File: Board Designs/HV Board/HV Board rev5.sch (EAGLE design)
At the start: 95 parts, among them IC1 OKI-78SR, IC2 NE5532SOIC, IC3 NE5532SOIC

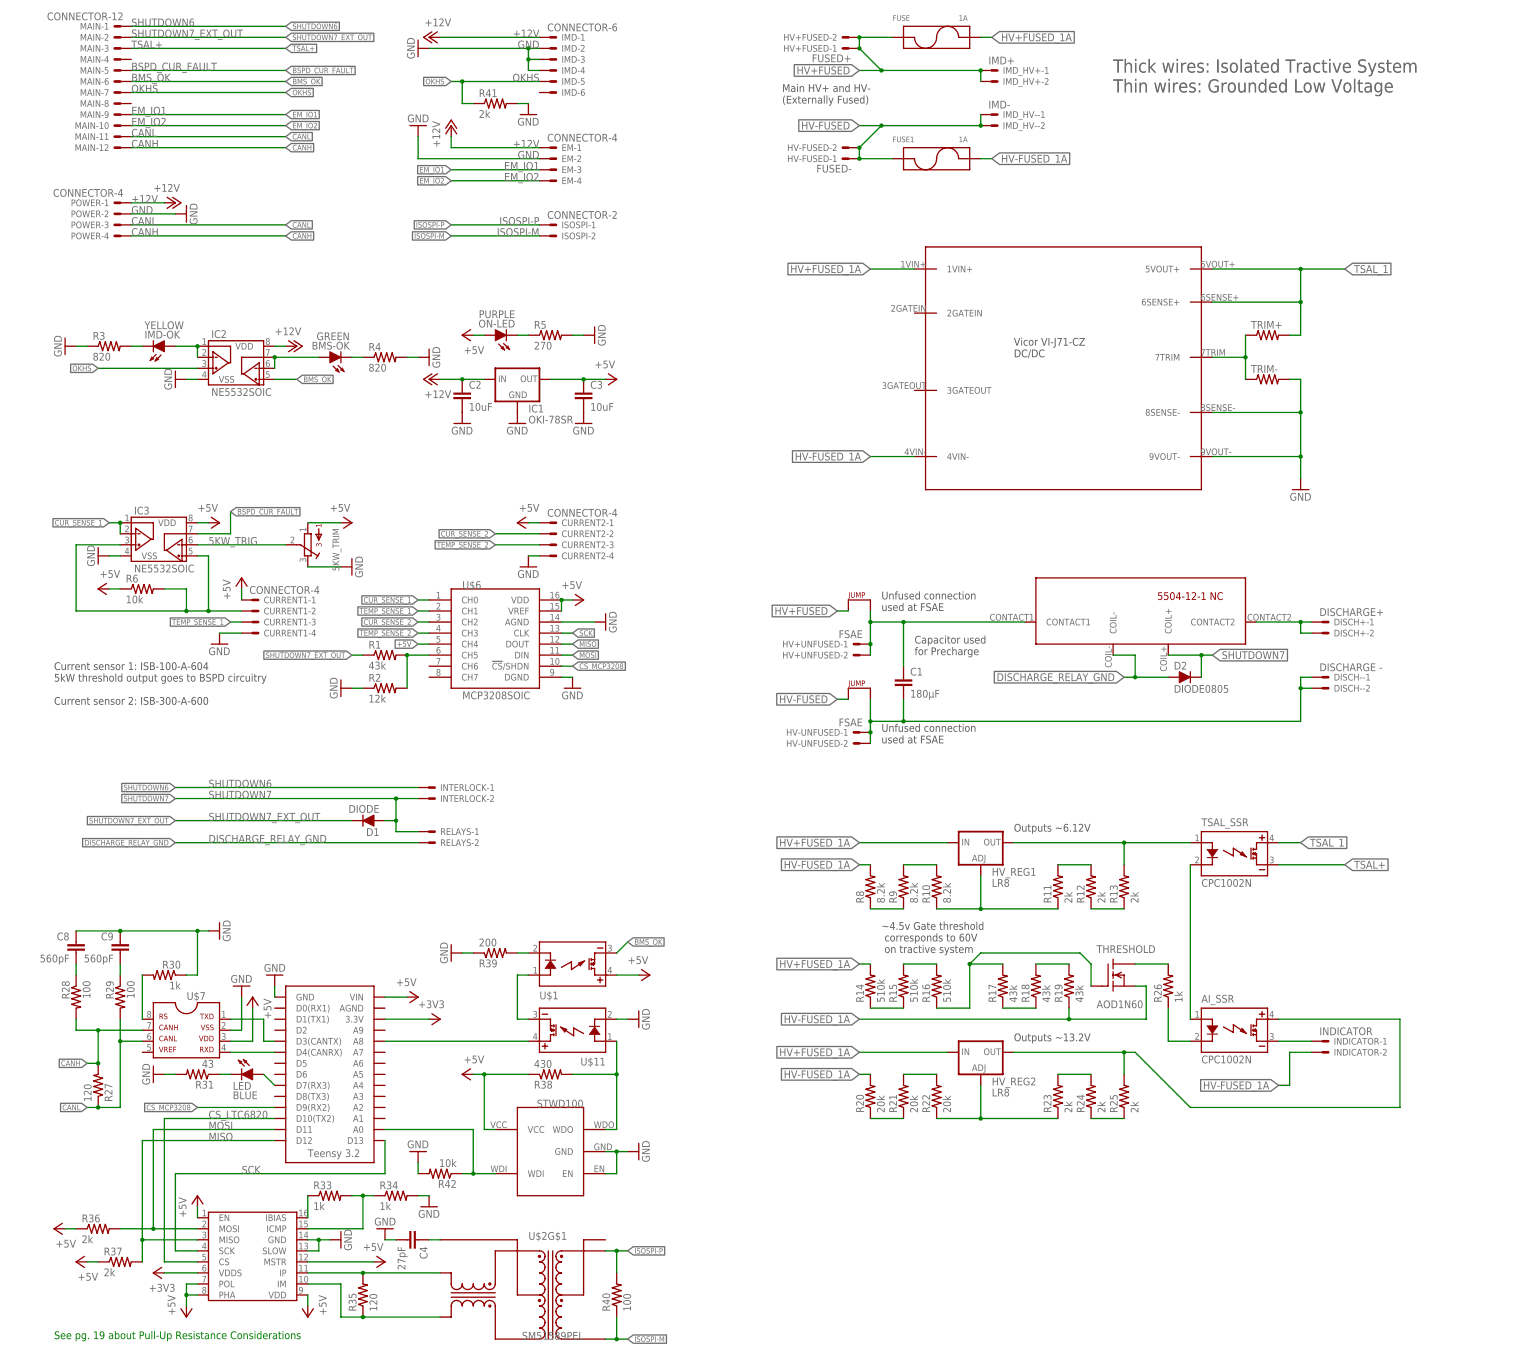
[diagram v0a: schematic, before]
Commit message: HV board redesign
Removed one SSR in BMS, BSPD current sensor, jumper for fused/unfused, TSAL 60Vmin circuit, accumulator indicator, and energy meter connector. Connected output of DC/DC converter straight to TSAL out. Added 8th order butterworth filter to current sensor, replaced some mini-fit connectors to nano-fit.
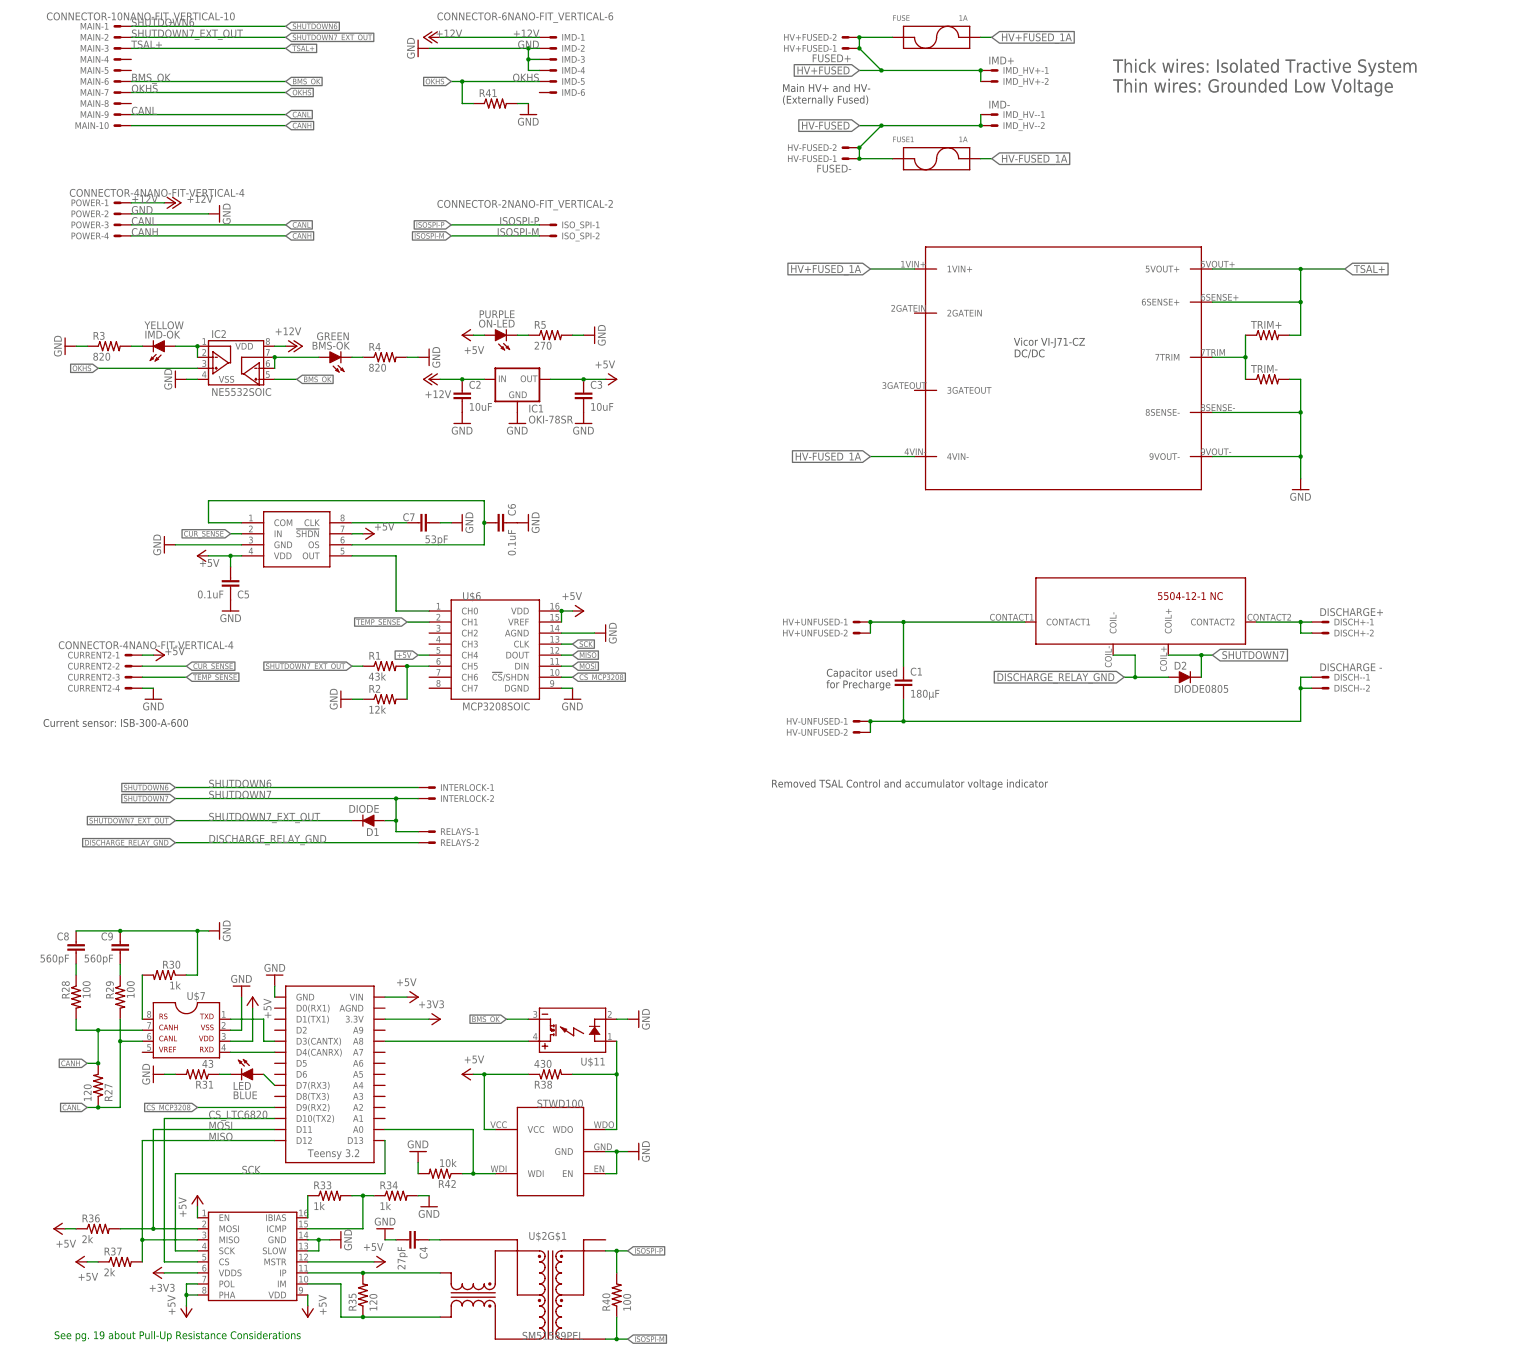
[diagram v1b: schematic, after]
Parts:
- removed 5KW_TRIM: (no value), HyTechDevices:TRIMPOT_3296C
- removed AI_SSR, TSAL_SSR: CPC1002N, HyTechDevices:CPC1002N
- removed CURRENT1: CONNECTOR-4, HyTechDevices:CONNECTOR-4
- removed EM: CONNECTOR-4, HyTechDevices:CONNECTOR-4NANO-FIT-VERTICAL-4
- removed HV_REG1, HV_REG2: LR8, HyTechDevices:HV_LIN_REG_LR8SMD
- removed IC3: NE5532SOIC, HyTechDevices:NE5532SOIC
- removed INDICATOR: INDICATOR, HyTechDevices:MINIFIT_5566-2
- removed R10, R8, R9: 8.2k, HyTechDevices:RESISTOR0805-RES
- removed R11, R12, R13, R23, R24, R25: 2k, HyTechDevices:RESISTOR0805-RES
- removed R14, R15, R16: 510k, HyTechDevices:RESISTOR0805-RES
- removed R17, R18, R19: 43k, HyTechDevices:RESISTOR0805-RES
- removed R20, R21, R22: 20k, HyTechDevices:RESISTOR0805-RES
- removed R26: 1k, HyTechDevices:RESISTOR0805-RES
- removed R39: 200, HyTechDevices:RESISTOR0805-RES
- removed R6: 10k, HyTechDevices:RESISTOR0805-RES
- removed THRESHOLD: AOD1N60, HyTechDevices:N-CHANNEL_MOSFETAOD1N60
- removed U$3, U$4: JUMPER.3, HyTechDevices:JUMPER.3
- added C5, C6: 0.1uF, HyTechDevices:CAP0805
- added C7: 53pF, HyTechDevices:CAP0805
- CURRENT2, POWER: value CONNECTOR-4 -> CONNECTOR-4NANO-FIT-VERTICAL-4; device HyTechDevices:CONNECTOR-4 -> HyTechDevices:CONNECTOR-4NANO-FIT-VERTICAL-4
- HV-UNFUSED: value FSAE -> HV_UNFUSED
- IMD: value CONNECTOR-6 -> CONNECTOR-6NANO-FIT_VERTICAL-6
- ISO_SPI: value CONNECTOR-2 -> CONNECTOR-2NANO-FIT_VERTICAL-2
- MAIN: value CONNECTOR-12 -> CONNECTOR-10NANO-FIT_VERTICAL-10; device HyTechDevices:CONNECTOR-12 -> HyTechDevices:CONNECTOR-10NANO-FIT_VERTICAL-10
- U$1: value CPC1002N -> (none); device HyTechDevices:CPC1002N -> HyTechDevices:MAX7480
- renumbered ISOSPI to ISO_SPI
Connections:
- removed net 5KW_TRIG: 5KW_TRIM.2, IC3.VINB-
- removed net BMS_WATCH: U$1.CONTROL+, U$11.DC-
- removed net BSPD_CUR_FAULT: IC3.VOUTB, MAIN-5.S
- removed net CUR_SENSE_1: IC3.VINA-, IC3.VOUTA, U$6.CH0
- removed net CUR_SENSE_1_RAW: CURRENT1-2.S, IC3.VINA+, IC3.VINB+, R6.2
- removed net CUR_SENSE_2: CURRENT2-2.S, U$6.CH2
- removed net EM_IO1: EM-3.S, MAIN-9.S
- removed net EM_IO2: EM-4.S, MAIN-10.S
- removed net N$10: R14.1, R15.1
- removed net N$11: R15.2, R16.2
- removed net N$12: R17.1, R18.1
- removed net N$13: R18.2, R19.2
- removed net N$14: R10.2, R9.2
- removed net N$15: HV_REG2.ADJ, R22.1, R23.1
- removed net N$16: R11.2, R12.2
- removed net N$17: R12.1, R13.1
- removed net N$18: HV_REG1.ADJ, R10.1, R11.1
- removed net N$19: R23.2, R24.2
- removed net N$20: R24.1, R25.1
- removed net N$21: R21.2, R22.2
- removed net N$22: R16.1, R17.2, THRESHOLD.G
- removed net N$23: R20.1, R21.1
- removed net N$5: AI_SSR.CONTROL-, R26.1
- removed net N$6: AI_SSR.CONTROL+, TSAL_SSR.CONTROL-
- removed net N$7: AI_SSR.DC-, INDICATOR-1.S
- removed net N$8: R8.1, R9.1
- removed net N$9: R26.2, THRESHOLD.D
- removed net TEMP_SENSE_1: CURRENT1-3.S, U$6.CH1
- removed net TEMP_SENSE_2: CURRENT2-3.S, U$6.CH3
- removed net TSAL_1: TRIM+.2, TSAL_SSR.DC+, U$5.5VOUT+, U$5.6SENSE+
- new net CUR_SENSE: CURRENT2-2.S, U$1.IN
- new net TEMP_SENSE: CURRENT2-3.S, U$6.CH1
- net +12V: no longer EM-1.S
- net +5V: now also C5.1, U$1.!SHDN, U$1.VDD; no longer 5KW_TRIM.1, CURRENT1-1.S, IC3.VDD, R6.1, U$1.DC+
- net BMS_OK: now also U$11.DC-; no longer U$1.DC-
- net CANH: now also MAIN-10.S; no longer MAIN-12.S
- net CANL: now also MAIN-9.S; no longer MAIN-11.S
- net GND: now also C5.2, C6.2, C7.2, U$1.GND; no longer 5KW_TRIM.3, CURRENT1-4.S, EM-2.S, IC3.VSS, R39.1
- net HV+FUSED: no longer U$3.P$1
- net HV+FUSED_1A: no longer HV_REG1.IN, HV_REG2.IN, R14.2
- net HV+UNFUSED_FSAE: no longer U$3.P$2
- net HV-FUSED: no longer U$4.P$1
- net HV-FUSED_1A: no longer INDICATOR-2.S, R19.1, R20.2, R8.2, THRESHOLD.S
- net HV-UNFUSED_FSAE: no longer U$4.P$2
- net N$1: now also U$1.OUT, U$6.CH0; no longer AI_SSR.DC+, HV_REG2.OUT, R25.2
- net N$2: now also C6.1, U$1.COM, U$1.OS; no longer HV_REG1.OUT, R13.2, TSAL_SSR.CONTROL+
- net N$4: now also C7.1, U$1.CLK; no longer R39.2, U$1.CONTROL-
- net TSAL+: now also TRIM+.2, U$5.5VOUT+, U$5.6SENSE+; no longer TSAL_SSR.DC-
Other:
- note added: "Current sensor: ISB-300-A-600"
- note added: "Removed TSAL Control and accumulator voltage indicator"
- note removed: "Current sensor 1: ISB-100-A-604 5kW threshold output goes to BSPD circuitry Current sensor 2: ISB-300-A-600"
- note removed: "Outputs ~13.2V"
- note removed: "Outputs ~6.12V"
- note removed: "TSAL Control, Accumulator Voltage Indicator"
- note removed: "Unfused connection used at FSAE"
- note removed: "~4.5v Gate threshold corresponds to 60V on tractive system"
- moved on the sheet: CURRENT2-1, CURRENT2-2, CURRENT2-3, CURRENT2-4, HV+UNFUSED-1, HV+UNFUSED-2, HV-UNFUSED-1, HV-UNFUSED-2, R1, R2, U$6
